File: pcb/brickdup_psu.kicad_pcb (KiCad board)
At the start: 2 copper layers, 40 x 20 mm, 23 parts, among them J1 VBAT/GND (JST PH), J2 5V/SENSE/GND (JST PH), U1 MP9486A

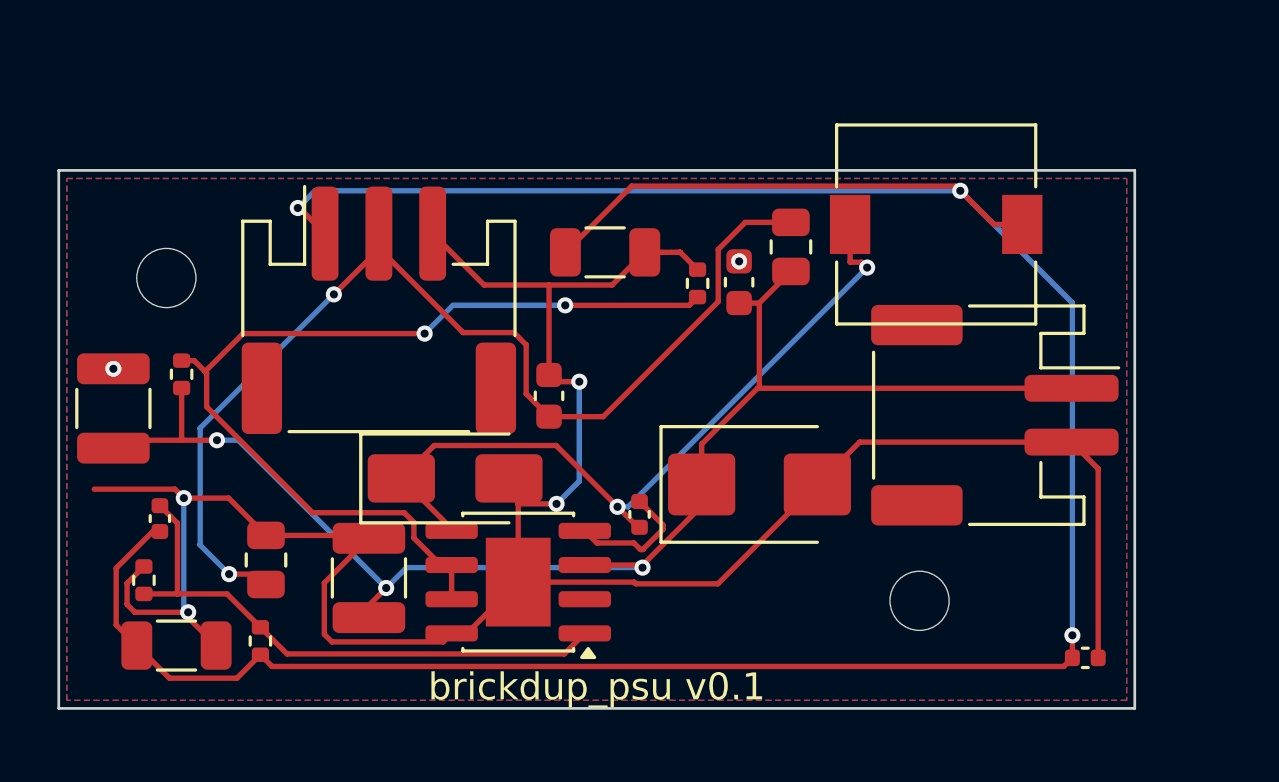
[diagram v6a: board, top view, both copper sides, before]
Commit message: pcb: swap L1 to 12mm 3A inductor (CYH127-33UH) + re-route
The previous 7.3mm L1 footprint could only take ~1.2A inductors, which would
saturate at the 1.30A peak. Swap to a real adequate part: SHOU HAN CYH127-33UH
(C2929502, 33uH / 3A) on the matching L_12x12mm_H8mm footprint, and re-run
place+route. Moved the M2 mounting holes to the south band (clear of the J2/J1
connector edges) and the enclosure J2 wire-notch to match J2's new position.

Board: 0 unconnected, 0 shorts (routed the one stranded VBAT pad on B.Cu,
removed GND-pour islands). DRC 34 = cosmetic silk + warnings; note the bigger
inductor crowds the board (11 courtyard-overlap warnings). Enclosure recompiles;
fab/ + render + BOM (L1 = C2929502) regenerated.

Co-Authored-By: Claude Opus 4.8 <noreply@anthropic.com>
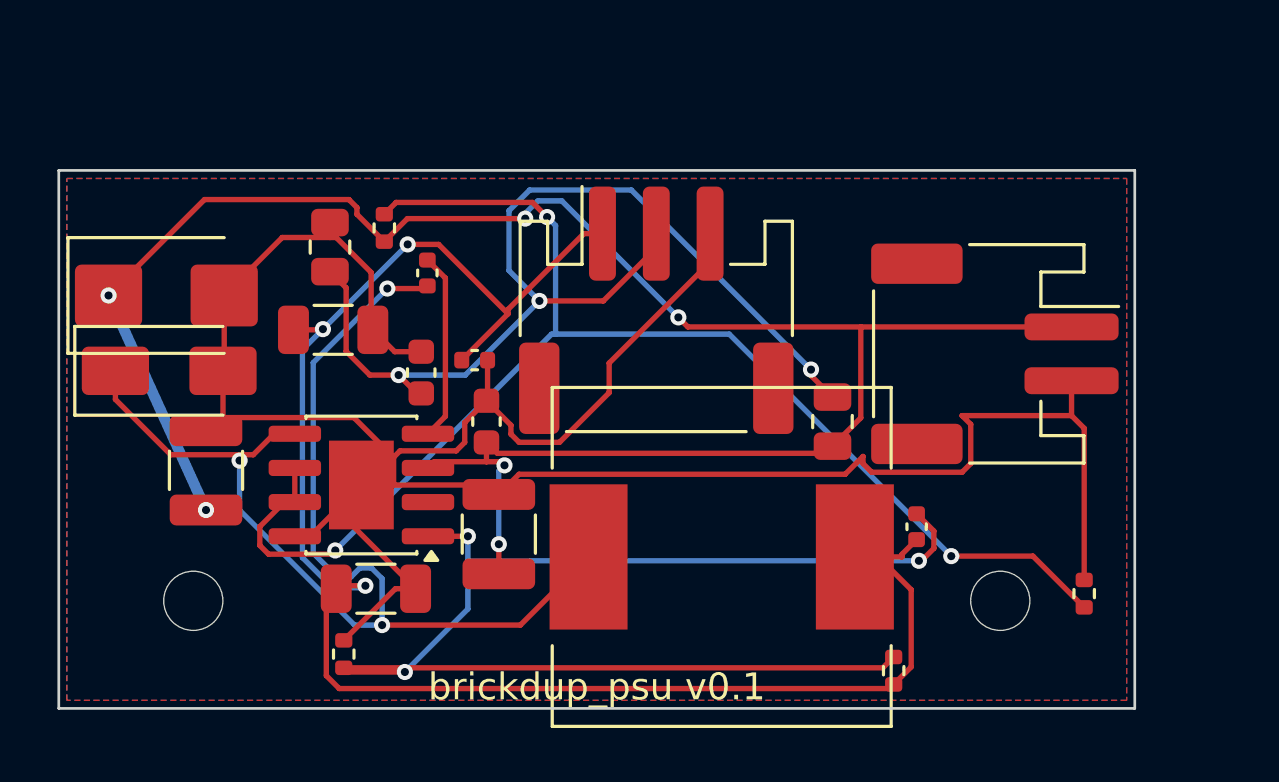
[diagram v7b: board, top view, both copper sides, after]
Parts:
- L1: value 33uH -> 33uH 3A; footprint L_7.3x7.3_H4.5 -> L_12x12mm_H8mm
- moved Cff 28.1 mm to (31.9, 13.2)
- moved Cout3 25.3 mm to (15.5, 7.05)
- moved RFB1 23.6 mm to (31.0, 18.6)
- moved D2 23.1 mm to (4.00, 4.65)
- moved REN2 18.4 mm to (38.1, 15.7)
- moved Cout2 15.1 mm to (11.8, 15.6)
- moved Cin1 15.1 mm to (16.4, 13.5)
- moved L1 14.7 mm to (24.6, 14.4)
- moved Cout1 13.1 mm to (10.2, 5.93)
- moved H1 12.0 mm to (5.00, 16.0)
- moved Cbst 11.9 mm to (13.7, 3.81)
- moved R2 11.9 mm to (10.1, 2.85)
- moved D1 11.4 mm to (4.11, 7.45)
- moved Cin3 10.7 mm to (15.9, 9.34)
- moved J2 10.3 mm to (22.2, 5.20)
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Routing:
- net +5V: track 105.3 -> 63.3 mm
- net FB: track 21.2 -> 49.5 mm, vias 0 -> 3
- net VBAT: track 53.5 -> 75.4 mm, vias 3 -> 6
- net EN: track 35.0 -> 53.0 mm, vias 2 -> 3
- net SW: track 28.4 -> 44.2 mm, vias 2 -> 3
- net GND: track 91.0 -> 93.4 mm, vias 6 -> 0
- net SENSE: track 40.5 -> 38.2 mm, vias 2 -> 3
- net BST: track 4.90 -> 7.00 mm

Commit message: pcb: switch L1 to CYA0850 (9.2x8mm, 6A) on a custom footprint
Replace the crowding 12.3mm CYH127 with SHOU HAN CYA0850-33UH (C19268648):
33uH, 3A rated / 6A saturation, 9.2x8mm molded -- smaller AND much higher
current margin (6A sat vs 1.30A peak). Added a correct project-local footprint
pcb/brickdup.pretty/L_CYA0850 (2-pad, 9.2x8 land) and taught gen_pcb to load
project footprints.

Re-ran place+route: fully routed, **0 unconnected, 0 shorts**, no isolated
copper, no manual fixups. Courtyard-overlap warnings down 11 -> 7; remaining
31 DRC are cosmetic silk + 7 courtyard warnings. Regenerated fab/ + render;
BOM L1 = C19268648.

Co-Authored-By: Claude Opus 4.8 <noreply@anthropic.com>
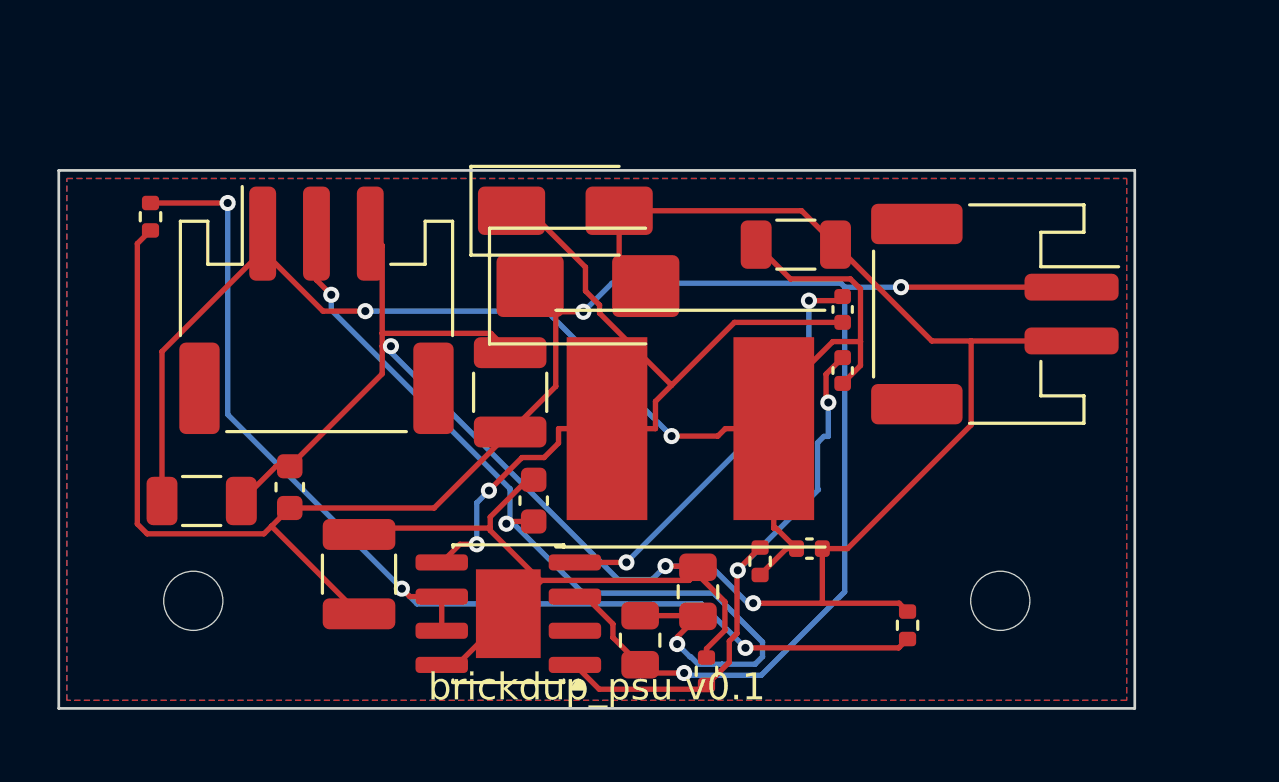
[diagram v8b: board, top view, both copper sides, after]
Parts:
- L1: value 33uH 3A -> 33uH 6A; footprint L_12x12mm_H8mm -> L_CYA0850
- moved Cout2 20.2 mm to (27.4, 2.76)
- moved R2 18.7 mm to (23.8, 15.7)
- moved D1 15.9 mm to (18.8, 1.50)
- moved D2 15.7 mm to (19.7, 4.30)
- moved Cbst 15.5 mm to (29.1, 5.17)
- moved Cout3 14.3 mm to (27.9, 14.1)
- moved RFB2 13.5 mm to (24.1, 18.6)
- moved J2 12.6 mm to (9.58, 5.20)
- moved R1 10.8 mm to (21.6, 17.5)
- moved REN1 8.70 mm to (3.41, 1.72)
- moved Cout1 8.02 mm to (5.31, 12.3)
- moved Cin3 7.71 mm to (8.59, 11.8)
- moved U1 7.26 mm to (16.7, 16.5)
- moved Cin2 6.87 mm to (11.2, 15.0)
- moved REN2 6.67 mm to (31.6, 16.9)
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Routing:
- net FB: track 49.5 -> 21.0 mm, vias 3 -> 2
- net SW: track 44.2 -> 29.7 mm, vias 3 -> 2
- net EN: track 53.0 -> 42.6 mm
- net +5V: track 63.3 -> 53.6 mm, vias 3 -> 2
- net GND: track 93.4 -> 103.0 mm, vias 0 -> 3
- net BST: track 7.00 -> 15.8 mm, vias 0 -> 2
- net VBAT: track 75.4 -> 81.6 mm, vias 6 -> 3
- net SENSE: track 38.2 -> 33.8 mm
